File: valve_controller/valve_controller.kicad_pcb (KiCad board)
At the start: 4 copper layers, 171.6 x 85 mm, 93 parts, among them J1 T4132512041-000, J10 M12A-05PFFP-SF8001, J11 M12A-05PFFP-SF8001, J2 20021511-00006T4LF, J3 54-00384, J4 M12A-05PFFP-SF8001, J5 M12A-05PFFP-SF8001, J6 M12A-05PFFP-SF8001, J7 M12A-05PFFP-SF8001, J8 M12A-05PFFP-SF8001, J9 M12A-05PFFP-SF8001, U1 LAN8720A, U10 GP8403-TC50-EW, U11 AP2112K-3.3, U2 ESP32-WROOM-32, U3 LM2576S-12, U4 ADS1115IDGS, U5 GP8403-TC50-EW, U6 GP8403-TC50-EW, U7 ADS1115IDGS, U8 LM2576S-5, U9 GP8403-TC50-EW, Y1 ASE-25.000MHZ-LC-T

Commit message: First DRC run
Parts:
- moved R6 3.46 mm to (217.1, 112.6)
- moved R8 3.46 mm to (211.6, 112.6)
- moved D10 2.50 mm to (211.6, 109.2)
- moved D14 2.50 mm to (214.4, 84.2)
- moved D5 2.50 mm to (217.2, 109.2)
- moved R7 1.35 mm to (207.5, 108.4), turned to 90 degrees
- moved ? 1.24 mm to (139.4, 101.8)
- moved REF** 1.24 mm to (139.4, 101.8)
- moved ? 0.59 mm to (139.4, 91.7)
- moved REF** 0.59 mm to (139.4, 91.7)
- renumbered D21 to D10, D7 to D11, D17 to D12, D22 to D14, D14 to D15, D18 to D16, D8 to D17, D9 to D18, D10 to D19, D11 to D20, D19 to D21, D15 to D22, D20 to D5, D12 to D6, D16 to D7, D5 to D8, D6 to D9, R7 to R10, R4 to R3, R5 to R4, R6 to R5, R3 to R6, R9 to R7, R10 to R9
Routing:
- net /ESP_IO0: track 97.7 -> 131.2 mm, vias 2 -> 3
- net GND: track 118.4 -> 125.5 mm, vias 53 -> 55
- net /SDA: track 194.3 -> 201.3 mm, vias 6 -> 7
- net /LED2: track 51.6 -> 48.2 mm
- net /LED1: track 50.9 -> 53.8 mm
- net /SCL: track 203.3 -> 205.3 mm, vias 6 -> 7
- net /RGB_LED: track 16.1 -> 17.7 mm
- net Net-(D14-Pad2): track 1.81 -> 3.23 mm
- net Net-(D5-Pad1): track 3.30 -> 4.03 mm
- net Net-(D10-Pad1): track 3.32 -> 4.00 mm
- net unconnected-(U2-IO2-Pad24): track 0.53 -> 0.00 mm

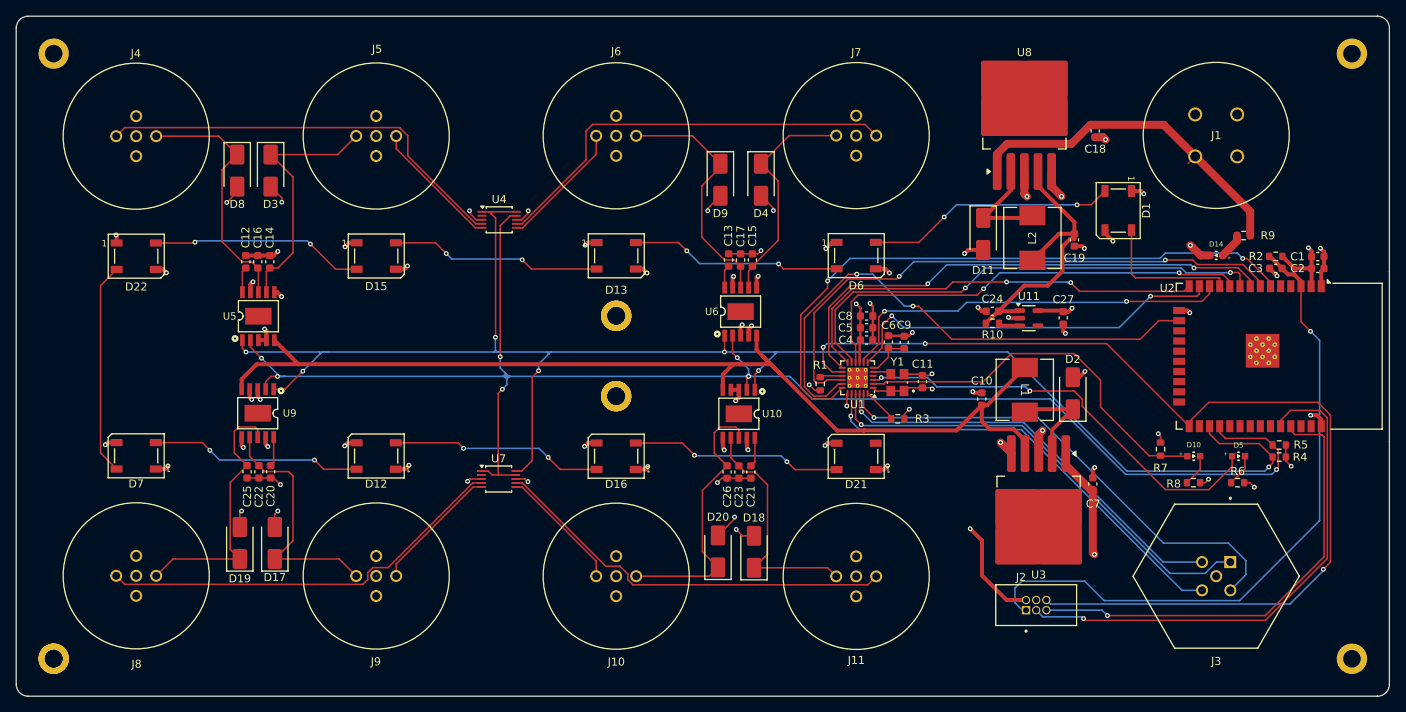
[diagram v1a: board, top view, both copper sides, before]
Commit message: New ethernet and power routing
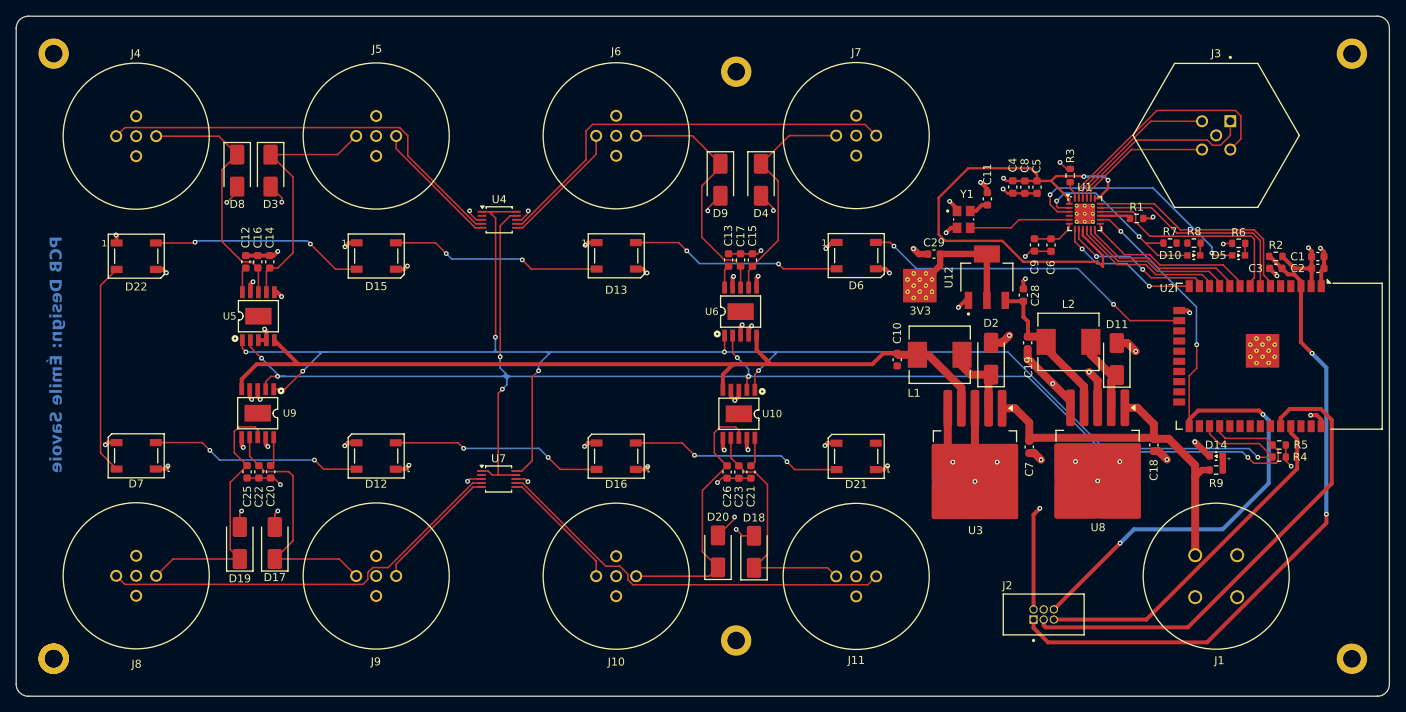
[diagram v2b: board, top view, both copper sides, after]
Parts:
- removed the ? at (139.4, 91.7)
- removed the ? at (139.4, 101.8)
- removed C24, C27: 22uF, Capacitor_SMD:C_0603_1608Metric
- removed D1: WS2812B, LED_SMD:LED_WS2812B_PLCC4_5.0x5.0mm_P3.2mm
- removed R10: 100k, Resistor_SMD:R_0603_1608Metric
- removed U11: AP2112K-3.3, Package_TO_SOT_SMD:SOT-23-5
- added ?: , , F.Cu at (175.9, 87.2)
- added ?: , , F.Cu at (176.6, 89.5)
- added ?: , , F.Cu at (175.9, 88.7)
- added ?: , , F.Cu at (178.1, 89.5)
- added ?: , , F.Cu at (178.9, 87.2)
- added ?: , , F.Cu at (178.9, 88.7)
- added ?: , , F.Cu at (176.6, 86.4)
- added ?: , , F.Cu at (177.4, 87.9)
- added ?: , , F.Cu at (176.6, 87.9)
- added ?: , , F.Cu at (178.1, 87.9)
- added ?: , , F.Cu at (178.1, 86.4)
- added ?: , , F.Cu at (177.4, 87.2)
- added ?: , , F.Cu at (177.4, 88.7)
- added C28: 1uF, Capacitor_SMD:C_0603_1608Metric, F.Cu at (190.3, 89.1)
- added C29: 1uF, Capacitor_SMD:C_0603_1608Metric, F.Cu at (179.1, 84.0)
- added U12: TLV1117LV33DCYR, TLV1117LV33DCYR:VREG_TLV1117LV33DCYR, F.Cu at (185.8, 86.9)
- moved J1 60.3 mm to (217.0, 126.9), turned to -90 degrees
- moved J3 55.1 mm to (214.4, 69.2)
- moved U8 45.8 mm to (199.6, 110.8), turned to -90 degrees
- moved R1 44.6 mm to (204.5, 79.5), turned to 0 degrees
- moved C18 39.9 mm to (206.6, 107.8)
- moved R3 37.3 mm to (196.2, 74.2), turned to -90 degrees
- moved U1 35.0 mm to (198.0, 78.9), turned to 0 degrees
- moved REF** 34.0 mm to (154.4, 132.3)
- moved REF** 34.0 mm to (154.4, 61.2)
- moved R8 30.0 mm to (211.6, 82.6), turned to 180 degrees
- moved R6 29.9 mm to (217.2, 82.6), turned to 180 degrees
- moved R9 29.5 mm to (214.4, 111.0), turned to 0 degrees
- moved C5 27.6 mm to (192.0, 75.6), turned to 90 degrees
- moved C4 26.5 mm to (189.0, 75.6), turned to 90 degrees
- moved R7 25.8 mm to (208.7, 82.6), turned to 0 degrees
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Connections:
- ? pad 1: (no net) -> GND
- D6 pad 4: /LED_01 -> /RGB_LED
- REF** pad 1: (no net) -> GND (x4)
- U2 pad 10: /RXER -> /MDIO
- U2 pad 11: /RGB_LED -> /CRS_DV
- U2 pad 12: /RXD0 -> /RXER
- U2 pad 13: /RXD1 -> /RXD0
- U2 pad 14: /MDIO -> /RXD1
- U2 pad 16: /TXD0 -> /RGB_LED
- U2 pad 7: /TXEN -> /TXD0
- U2 pad 8: /MDC -> /TXEN
- U2 pad 9: /CRS_DV -> /MDC
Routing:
- net +3V3: track 77.9 -> 141.3 mm, vias 26 -> 25
- net /TXD1: track 79.9 -> 28.5 mm, vias 2 -> 0
- net /ESP_IO0: track 131.2 -> 84.9 mm, vias 3 -> 4
- net /TXEN: track 72.4 -> 27.3 mm, vias 2 -> 0
- net /MDC: track 64.7 -> 21.5 mm, vias 2 -> 0
- net /CRS_DV: track 62.0 -> 19.7 mm, vias 2 -> 0
- net /TXD0: track 67.8 -> 27.4 mm, vias 2 -> 0
- net /TX_N: track 56.2 -> 17.0 mm, vias 1 -> 0
- net /RXER: track 57.6 -> 19.0 mm, vias 2 -> 0
- net /TX_P: track 58.6 -> 24.1 mm, vias 1 -> 0
- net /MDIO: track 54.3 -> 20.6 mm, vias 2 -> 0
- net /RX_N: track 52.8 -> 19.6 mm, vias 1 -> 0
- net /RX_P: track 62.0 -> 30.5 mm, vias 1 -> 0
- net /LED_01: track 31.3 -> 0.00 mm, vias 2 -> 0
- net /RXD0: track 50.0 -> 19.0 mm
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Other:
- board text added: "3V3"
- board text added: "PCB Design: Émile Savoie"

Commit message: Changes after review
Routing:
- net GND: track 139.9 -> 149.2 mm, vias 55 -> 54
- net +3V3: track 141.3 -> 142.8 mm, vias 25 -> 26

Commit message: Updated changes for review
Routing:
- net +3V3: track 142.8 -> 141.4 mm
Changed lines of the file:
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@@
 			(solder_mask_margin 0.102)
 		)
+		(model "${CUSTOM}/20021511_00006T4LF/20021511-00006T4LF.step"
+			(offset
+				(xyz 0 0 0)
+			)
+			(scale
+				(xyz 1 1 1)
+			)
+			(rotate
+				(xyz -90 0 0)
+			)
+		)
 	)
 	(footprint ""
@@
 			(pintype "unspecified")
 		)
+		(model "${CUSTOM}/SRP6530A_100M/IND_SRP6530A_BRN.step"
+			(offset
+				(xyz 0 0 0)
+			)
+			(scale
+				(xyz 1 1 1)
+			)
+			(rotate
+				(xyz 0 0 0)
+			)
+		)
 	)
 	(footprint ""
@@
 			(solder_mask_margin 0.102)
 		)
+		(model "${CUSTOM}/ASE-25.000MHZ-LC-T/ASE-25.000MHZ-LC-T.step"
+			(offset
+				(xyz 0 0 0)
+			)
+			(scale
+				(xyz 1 1 1)
+			)
+			(rotate
+				(xyz -90 0 0)
+			)
+		)
 	)
 	(footprint "MountingHole:MountingHole_2.2mm_M2_DIN965_Pad"
@@
 			(pintype "unspecified+no_connect")
 		)
+		(model "${CUSTOM}/M12A_05PFFP_SF8001/M12A-05PFFP-SF8001.STEP"
+			(offset
+				(xyz 0 -13 0)
+			)
+			(scale
+				(xyz 1 1 1)
+			)
+			(rotate
+				(xyz 0 90 0)
+			)
+		)
 	)
 	(footprint "GP8403:ESSOP-10_L4.9-W3.9-P1.00-LS6.0-BL-EP"
@@
 			(pintype "unspecified+no_connect")
 		)
+		(model "${CUSTOM}/M12A_05PFFP_SF8001/M12A-05PFFP-SF8001.STEP"
+			(offset
+				(xyz 0 -13 0)
+			)
+			(scale
+				(xyz 1 1 1)
+			)
+			(rotate
+				(xyz 0 90 0)
+			)
+		)
 	)
 	(footprint "Diode_SMD:D_SMA"
@@
 			(pintype "unspecified")
 		)
+		(model "${CUSTOM}/SRP6530A_100M/IND_SRP6530A_BRN.step"
+			(offset
+				(xyz 0 0 0)
+			)
+			(scale
+				(xyz 1 1 1)
+			)
+			(rotate
+				(xyz 0 0 0)
+			)
+		)
 	)
 	(footprint "Resistor_SMD:R_0603_1608Metric"
@@
 			(pintype "unspecified+no_connect")
 		)
+		(model "${CUSTOM}/M12A_05PFFP_SF8001/M12A-05PFFP-SF8001.STEP"
+			(offset
+				(xyz 0 -13 0)
+			)
+			(scale
+				(xyz 1 1 1)
+			)
+			(rotate
+				(xyz 0 90 0)
+			)
+		)
 	)
 	(footprint "150060VS75000:WL-SMCW_0603"
@@
 			(pintype "unspecified+no_connect")
 		)
+		(model "${CUSTOM}/M12A_05PFFP_SF8001/M12A-05PFFP-SF8001.STEP"
+			(offset
+				(xyz 0 -13 0)
+			)
+			(scale
+				(xyz 1 1 1)
+			)
+			(rotate
+				(xyz 0 90 0)
+			)
+		)
 	)
 	(footprint "Capacitor_SMD:C_0603_1608Metric"
@@
 			(pintype "unspecified+no_connect")
 		)
+		(model "${CUSTOM}/M12A_05PFFP_SF8001/M12A-05PFFP-SF8001.STEP"
+			(offset
+				(xyz 0 -13 0)
+			)
+			(scale
+				(xyz 1 1 1)
+			)
+			(rotate
+				(xyz 0 90 0)
+			)
+		)
 	)
 	(footprint "TLV1117LV33DCYR:VREG_TLV1117LV33DCYR"
@@
 			(solder_mask_margin 0.102)
 		)
+		(model "${CUSTOM}/TLV1117LV33DCYR/TLV1117LV33DCYR.step"
+			(offset
+				(xyz 0 0 0)
+			)
+			(scale
+				(xyz 1 1 1)
+			)
+			(rotate
+				(xyz -90 0 0)
+			)
+		)
 	)
 	(footprint "M12A_05footprints:CONN_SF8001_AMP"
@@
 			(pintype "unspecified+no_connect")
 		)
+		(model "${CUSTOM}/M12A_05PFFP_SF8001/M12A-05PFFP-SF8001.STEP"
+			(offset
+				(xyz 0 -13 0)
+			)
+			(scale
+				(xyz 1 1 1)
+			)
+			(rotate
+				(xyz 0 90 0)
+			)
+		)
 	)
 	(footprint "Resistor_SMD:R_0603_1608Metric"
@@
 			(pintype "unspecified+no_connect")
 		)
+		(model "${CUSTOM}/M12A_05PFFP_SF8001/M12A-05PFFP-SF8001.STEP"
+			(offset
+				(xyz 0 -13 0)
+			)
+			(scale
+				(xyz 1 1 1)
+			)
+			(rotate
+				(xyz 0 90 0)
+			)
+		)
 	)
 	(footprint "LED_SMD:LED_WS2812B_PLCC4_5.0x5.0mm_P3.2mm"
@@
 			)
 		)
+		(model "${CUSTOM}/LAN8720A_CP/LAN8720A-CP.step"
+			(offset
+				(xyz 0 0 0)
+			)
+			(scale
+				(xyz 1 1 1)
+			)
+			(rotate
+				(xyz -90 0 0)
+			)
+		)
 	)
 	(footprint "MountingHole:MountingHole_2.2mm_M2_DIN965_Pad"
@@
 	)
 	(segment
+		(start 200.111496 84.557743)
+		(end 200.111496 84.019264)
+		(width 0.3)
+		(layer "F.Cu")
+		(net 1)
+	)
+	(segment
+		(start 192.03 74.845)
+		(end 192.03 74.09)
+		(width 0.3)
+		(layer "F.Cu")
+		(net 1)
+	)
+	(segment
 		(start 155.75985 106.9501)
 		(end 155.75985 108.3)
@@
 	)
 	(segment
-		(start 187.680761 82.33)
-		(end 190.290761 84.94)
-		(width 0.3)
-		(layer "F.Cu")
-		(net 1)
-	)
-	(segment
 		(start 155.75985 108.3)
 		(end 155.90985 108.45)
@@
 	)
 	(segment
+		(start 199.729239 84.94)
+		(end 200.111496 84.557743)
+		(width 0.3)
+		(layer "F.Cu")
+		(net 1)
+	)
+	(segment
 		(start 95.60985 107.7749)
 		(end 95.88485 108.0499)
@@
 	)
 	(segment
-		(start 191.2 73.26)
-		(end 183.42 73.26)
-		(width 0.3)
-		(layer "F.Cu")
-		(net 1)
-	)
-	(segment
 		(start 76.98 81.675079)
 		(end 76.904965 81.600044)
@@
 	)
 	(segment
+		(start 190.290761 84.94)
+		(end 199.729239 84.94)
+		(width 0.3)
+		(layer "F.Cu")
+		(net 1)
+	)
+	(segment
 		(start 93.7 87.775)
 		(end 94.025 87.45)
@@
 	)
 	(segment
-		(start 197.75 81.657768)
-		(end 197.75 80.88)
-		(width 0.3)
-		(layer "F.Cu")
-		(net 1)
-	)
-	(segment
-		(start 200.27 84.177768)
-		(end 197.75 81.657768)
-		(width 0.3)
-		(layer "F.Cu")
-		(net 1)
-	)
-	(segment
 		(start 95.60985 106.8751)
 		(end 95.60985 107.7749)
@@
 	)
 	(segment
-		(start 190.290761 84.94)
-		(end 199.617008 84.94)
+		(start 179.73 81.53)
+		(end 180.53 82.33)
 		(width 0.3)
 		(layer "F.Cu")
@@
 	)
 	(segment
-		(start 224.2001 85.775)
-		(end 222.7 84.2749)
-		(width 0.5)
-		(layer "F.Cu")
-		(net 1)
-	)
-	(segment
-		(start 183.42 73.26)
-		(end 179.73 76.95)
+		(start 197.75 81.657768)
+		(end 197.75 80.88)
 		(width 0.3)
 		(layer "F.Cu")
@@
 	)
 	(segment
-		(start 192.03 74.09)
-		(end 191.2 73.26)
-		(width 0.3)
+		(start 224.2001 85.775)
+		(end 222.7 84.2749)
+		(width 0.5)
 		(layer "F.Cu")
 		(net 1)
@@
 	)
 	(segment
-		(start 182.03 78.31)
-		(end 181.11 77.39)
-		(width 0.5)
+		(start 187.680761 82.33)
+		(end 190.290761 84.94)
+		(width 0.3)
 		(layer "F.Cu")
 		(net 1)
 	)
 	(segment
-		(start 179.73 76.95)
-		(end 179.73 81.53)
-		(width 0.3)
+		(start 182.03 78.31)
+		(end 181.11 77.39)
+		(width 0.5)
 		(layer "F.Cu")
 		(net 1)
@@
 	)
 	(segment
-		(start 200.27 85.59)
-		(end 200.27 84.177768)
+		(start 192.03 74.09)
+		(end 191.2 73.26)
 		(width 0.3)
 		(layer "F.Cu")
@@
 	)
 	(segment
+		(start 180.53 82.33)
+		(end 187.680761 82.33)
+		(width 0.3)
+		(layer "F.Cu")
+		(net 1)
+	)
+	(segment
 		(start 128.430392 78.863236)
 		(end 128.430392 78.580392)
@@
 	)
 	(segment
+		(start 191.2 73.26)
+		(end 183.42 73.26)
+		(width 0.3)
+		(layer "F.Cu")
+		(net 1)
+	)
+	(segment
 		(start 192.03 74.845)
 		(end 193.795 74.845)
@@
 	)
 	(segment
+		(start 200.111496 84.019264)
+		(end 197.75 81.657768)
+		(width 0.3)
+		(layer "F.Cu")
+		(net 1)
+	)
+	(segment
 		(start 81.87 110.84998)
 		(end 83.019989 110.84998)
@@
 	)
 	(segment
-		(start 199.617008 84.94)
-		(end 199.618504 84.938504)
-		(width 0.3)
-		(layer "F.Cu")
-		(net 1)
-	)
-	(segment
-		(start 180.53 82.33)
-		(end 187.680761 82.33)
+		(start 183.42 73.26)
+		(end 179.73 76.95)
 		(width 0.3)
 		(layer "F.Cu")
@@
 	)
 	(segment
-		(start 192.03 74.845)
-		(end 192.03 74.09)
-		(width 0.3)
-		(layer "F.Cu")
-		(net 1)
-	)
-	(segment
 		(start 93.60985 101.8999)
 		(end 93.85985 102.1499)
@@
 	)
 	(segment
-		(start 199.618504 84.938504)
-		(end 200.27 85.59)
-		(width 0.3)
-		(layer "F.Cu")
-		(net 1)
-	)
-	(segment
 		(start 226.35 84.3)
 		(end 226.35 83.6)
@@
 	)
 	(segment
-		(start 179.73 81.53)
-		(end 180.53 82.33)
+		(start 179.73 76.95)
+		(end 179.73 81.53)
 		(width 0.3)
 		(layer "F.Cu")
